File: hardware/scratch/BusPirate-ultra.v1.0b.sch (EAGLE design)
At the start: 164 parts, among them IC1 IC_MEM_23LC1024, IC10 IC_BUFF_SN74LVC1T45DBV, IC11 IC_BUFF_SN74LVC1T45DBV, IC12 74LVC1G07DBV, IC13 IC_BUFF_SN74LVC1T45DBV, IC17 74LVC1G07DBV, IC18 IC_BUFF_SN74LVC1T45DBV, IC19 74LVC1G07DBV, IC2 IC_MEM_23LC1024, IC20 IC_BUFF_SN74LVC1T45DBV, IC21 74LVC1G07DBV, IC22 IC_BUFF_SN74LVC1T45DBV, IC23 MCP1824_ADJ, IC24 74HCT4051, IC3 IC_74AC573, IC4 74LVC1G07DBV, IC5 74LVC1G07DBV, IC6 74LVC1G07DBV, IC7 74LVC1G07DBV, IC8 SN74LVC1T45DBV, IC9 IC_BUFF_SN74LVC1T45DBV, J1 CON_HEADER_2X02-PTH, J2 CON_HEADER_1X04, J3 CON_HEADER_1X03-PTH, J4 CON_HEADER_1X10-RIGHT_ANGLED_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, Q1 DMMT3906W, U1 W25X40CL, U2 IC_UC_STM32F103ZX, U3 IC_FPGA_ICE40HX4K, U4 MCP6001, U5 MCP4442, U6 MCP4442

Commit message: fix placement
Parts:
- IC10, IC11, IC13, IC18, IC20, IC22, IC9: value IC_BUFF_SN74LVC1T45DBV -> SN74LVC1T45DBV
- U2: value IC_UC_STM32F103ZX -> STM32F103ZX
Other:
- note added: "FLASH STORAGE"
- note removed: "LA_LAT_MISO -> BPIO_MISO"
- moved on the sheet: C1, C10, C11, C12, C13, C14, C15, C16, C17, C18, C19, C2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

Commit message: changes are.. -fix schematic placements -wired latch chip to BP IO and fix net names -SRAM chip CS pin connected to ARM chip -flipped connection of BP IO, MOSI now on pin 1, GND on pin 10... etc -removed reset button -removed boot mode jumper config pins -buffer Vb connected to Vref/Vout -UART pins changed to test pads -EEPROM pins breakout to pads -ADC/Analog mux control pins wired to FPGA
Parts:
- removed J1: CON_HEADER_2X02-PTH, dp_devices:CON_HEADER_2X02-PTH
- removed J3: CON_HEADER_1X03-PTH, dp_devices.v6:CON_HEADER_1X03-PTH
- removed SW1: (no value), dp_devices.v6:SW_TACT_4P
- added C51: 1uF, rcl:C-EUC0603
- added D1: (no value), dp_devices.v6:DIODE-SOD-123
- added R50, R51: (no value), resistor:R-EU_R0603
- added TP1, TP2, TP3, TP4, TP5, TP6, TP7, TP8: TPB1,27, testpad:TPB1,27
- added U7: MCP6001, dp_devices.v6:IC_MCP6001
- IC1, IC2: value IC_MEM_23LC1024 -> 23LC1024
- IC3: value IC_74AC573 -> 74AC573
- U3: value IC_FPGA_ICE40HX4K -> ICE40HX4K
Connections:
- net LAT_SWV33 renamed LAT_AUX2
- net LAT_SWV50 renamed LAT_AUX3
- removed net BPIO_AUX: IC3IC.6D
- removed net LAT_CLK: IC3IC.3Q, U3BANK1.GBIN2/IOR_141
- removed net SWV33: IC3IC.7D
- removed net SWV50: IC3IC.8D
- removed net VPUN: C45.2, C46.2, C47.2, C48.2, C49.2, C56.2, C58.2, C60.2, IC10.VCCB, IC11.VCCB, IC13.VCCB, IC18.VCCB, IC20.VCCB, IC22.VCCB, IC8.VCCB, IC9.VCCB
- new net ADC_MUX_EN: IC24.!E, U3BANK2.IOB_73
- new net FLASH_CS: TP7.TP, U1.!CS, U2U.PG15/FT
- new net LAT_CLOCK: IC3IC.2Q, U3BANK1.GBIN3/IOR_140
- new net N$64: R51.1, U7.-, U7.OUT
- new net N$65: R51.2, R9.1
- net 3V3: no longer J1.2, J1.4, U1.!CS
- net ADC_MUX_S0: now also U3BANK2.IOB_64
- net ADC_MUX_S1: now also U3BANK2.IOB_71
- net ADC_MUX_S2: now also U3BANK2.IOB_72
- net BOOT0: no longer J1.1
- net BOOT1: no longer J1.3
- net BPIO_AUX0: now also IC3IC.5D, J4.5; no longer J4.6
- net BPIO_AUX1: now also IC3IC.6D, J4.6; no longer J4.5
- net BPIO_AUX2: now also IC3IC.7D, J4.7; no longer J4.4
- net BPIO_AUX3: now also IC3IC.8D, J4.8; no longer J4.3
- net BPIO_CLOCK: now also IC3IC.2D, J4.2; no longer IC3IC.3D, J4.9
- net BPIO_CS: now also IC3IC.4D, J4.4; no longer IC3IC.5D, J4.7
- net BPIO_MISO: now also IC3IC.3D, J4.3; no longer IC3IC.4D, J4.8
- net BPIO_MOSI: now also IC3IC.1D, J4.1; no longer IC3IC.2D, J4.10
- net FLASH_MISO: now also TP5.TP
- net FLASH_MOSI: now also TP4.TP
- net FLASH_SCK: now also TP6.TP
- net GND: now also C14.2, C51.2, IC24.VEE, J4.10, TP1.TP, TP8.TP, U7.V-; no longer C14.1, IC3IC.1D, J3.1, J4.1, SW1.3, SW1.4
- net LAT_AUX0: now also IC3IC.5Q, U3BANK1.IOR_146; no longer IC3IC.6Q, U3BANK1.IOR_147
- net LAT_AUX1: now also IC3IC.6Q, U3BANK1.IOR_147; no longer IC3IC.1Q, U3BANK1.IOR_139
- net LAT_CS: now also IC3IC.4Q, U3BANK1.IOR_144; no longer IC3IC.5Q, U3BANK1.IOR_146
- net LAT_MISO: now also IC3IC.3Q, U3BANK1.GBIN2/IOR_141; no longer IC3IC.4Q, U3BANK1.IOR_144
- net LAT_MOSI: now also IC3IC.1Q, U3BANK1.IOR_139; no longer IC3IC.2Q, U3BANK1.GBIN3/IOR_140
- net N$32: now also D1.A, R50.2, U7.+; no longer IC24.Z, R9.1
- net N$61: now also IC24.Z, R50.1; no longer U2U.PG15/FT
- net RST: no longer C14.2, SW1.1, SW1.2
- net UART_RX: now also TP2.TP; no longer J3.2
- net UART_TX: now also TP3.TP; no longer J3.3
- net VREF/VOUT: now also C45.2, C46.2, C47.2, C48.2, C49.2, C56.2, C58.2, C60.2, IC10.VCCB, IC11.VCCB, IC13.VCCB, IC18.VCCB, IC20.VCCB, IC22.VCCB, IC8.VCCB, IC9.VCCB, J4.9; no longer J4.2
- net VUSB: now also C14.1, C51.1, D1.C, U7.V+
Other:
- note added: "ADC MUX + Analog buffer"
- note added: "EEPROM"
- note added: "EEPROM TEST PADS"
- note removed: "ADC SENSE"
- note removed: "BOOT MODE"
- note removed: "FLASH STORAGE"
- note removed: "RESET"
- moved on the sheet: C1, C10, C11, C12, C13, C14, C15, C16, C17, C18, C19, C2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

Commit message: change BP IO to a more universal naming
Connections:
- net BPIO_AUX0 renamed BPIO4
- net BPIO_AUX1 renamed BPIO5
- net BPIO_AUX2 renamed BPIO6
- net BPIO_AUX3 renamed BPIO7
- net BPIO_CLOCK renamed BPIO1
- net BPIO_CS renamed BPIO3
- net BPIO_MISO renamed BPIO2
- net BPIO_MOSI renamed BPIO0
- net BUFDIR_AUX0 renamed BUFDIR4
- net BUFDIR_CLOCK renamed BUFDIR1
- net BUFDIR_CS renamed BUFDIR3
- net BUFDIR_MISO renamed BUFDIR2
- net BUFDIR_MOSI renamed BUFDIR0
- net BUFIO_AUX0 renamed BUFIO4
- net BUFIO_CLOCK renamed BUFIO1
- net BUFIO_CS renamed BUFIO3
- net BUFIO_MISO renamed BUFIO2
- net BUFIO_MOSI renamed BUFIO0
- net BUFOD_AUX0 renamed BUFOD4
- net BUFOD_CLOCK renamed BUFOD1
- net BUFOD_CS renamed BUFOD3
- net BUFOD_MISO renamed BUFOD2
- net BUFOD_MOSI renamed BUFOD0

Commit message: route new vreg circuit
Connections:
- net !SHDN renamed VREG_EN
- new net VREG_PWM: R48.2
- net PWM: no longer R48.2
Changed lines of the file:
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@@
 <label x="147.32" y="370.84" size="1.778" layer="95" align="center-left"/>
-</segment>
-<segment>
-<pinref part="R48" gate="R" pin="2"/>
-<label x="307.34" y="292.1" size="1.778" layer="95" align="center-right"/>
-<wire x1="309.88" y1="292.1" x2="307.34" y2="292.1" width="0.1524" layer="91"/>
 </segment>
 </net>
@@
 </segment>
 </net>
-<net name="!SHDN" class="0">
+<net name="VREG_EN" class="0">
 <segment>
 <pinref part="IC23" gate="IC" pin="!SHDN"/>
@@
 </segment>
 </net>
+<net name="VREG_PWM" class="0">
+<segment>
+<pinref part="R48" gate="R" pin="2"/>
+<label x="307.34" y="292.1" size="1.778" layer="95" align="center-right"/>
+<wire x1="309.88" y1="292.1" x2="307.34" y2="292.1" width="0.1524" layer="91"/>
+</segment>
+</net>

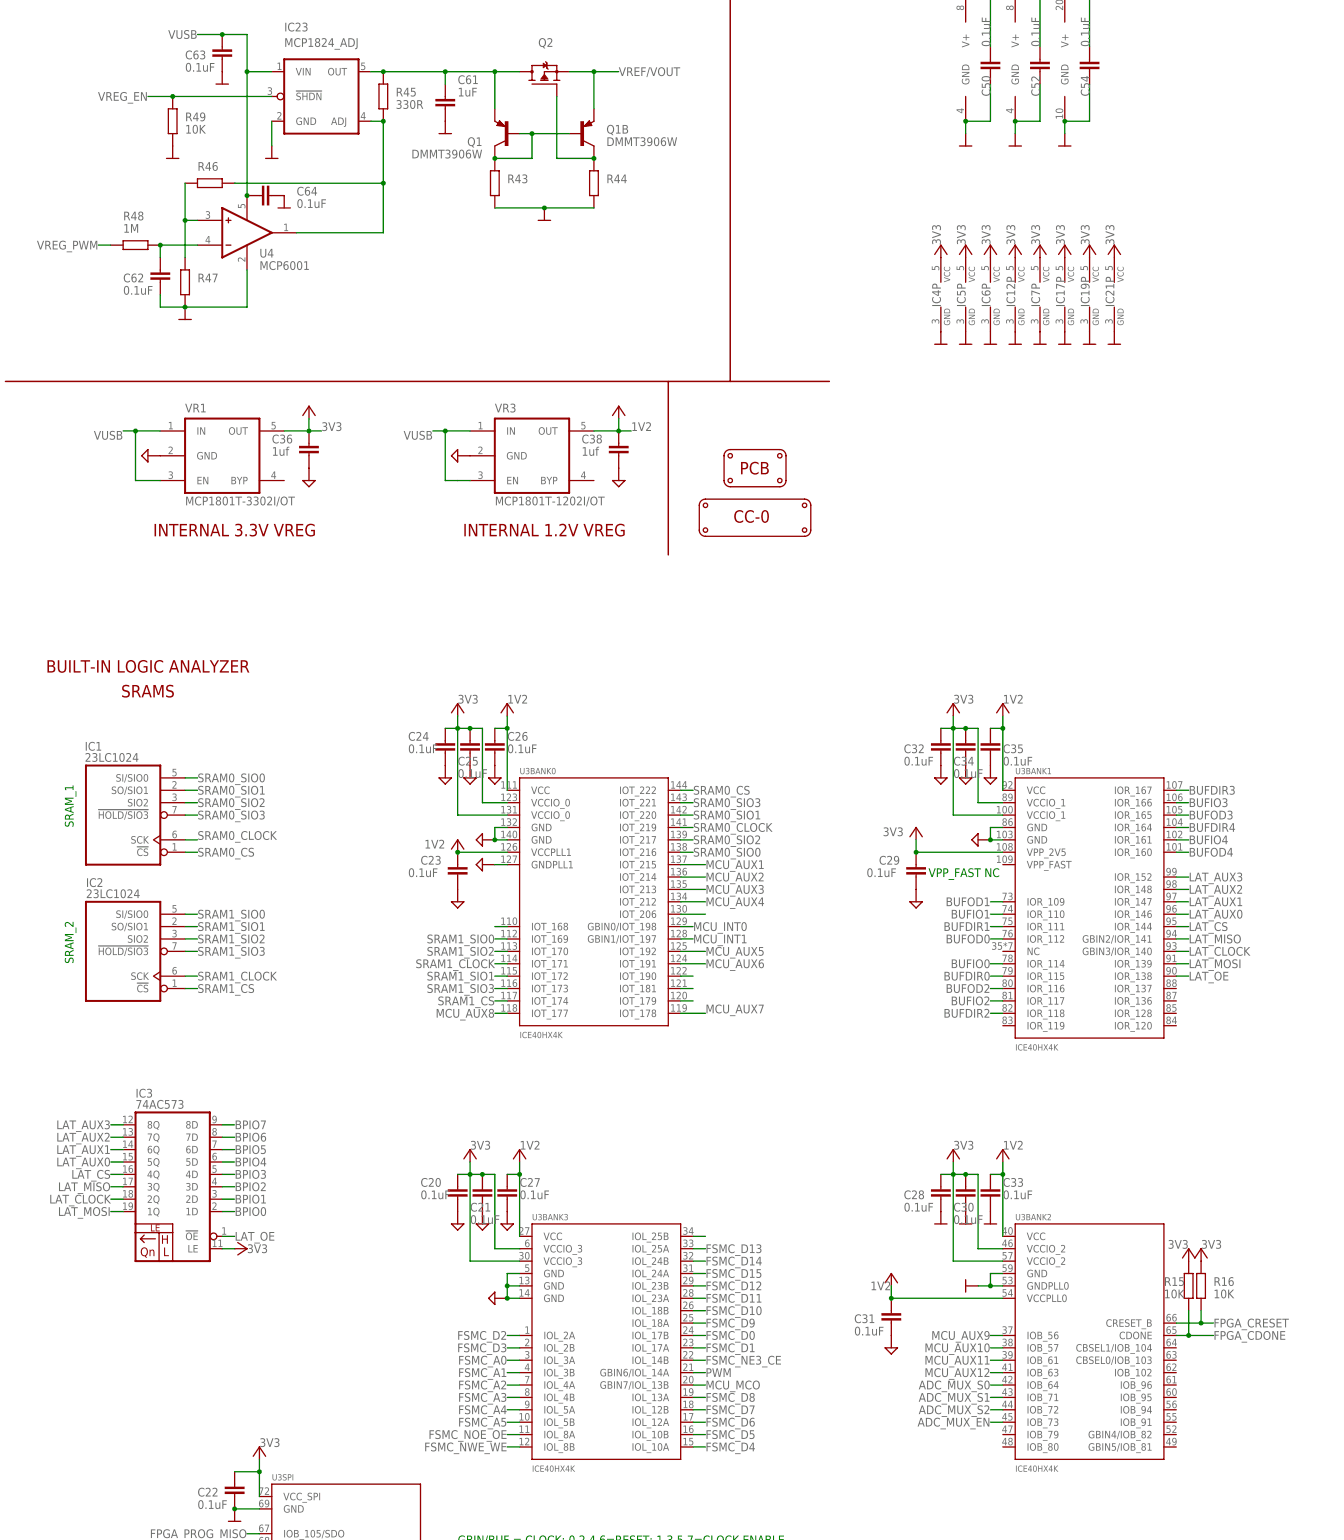
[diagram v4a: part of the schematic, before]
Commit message: move things around, move MCU_INT1 to GBIN5 and MCU_MCO to GBIN1, fix VREGEN and VREG_EN
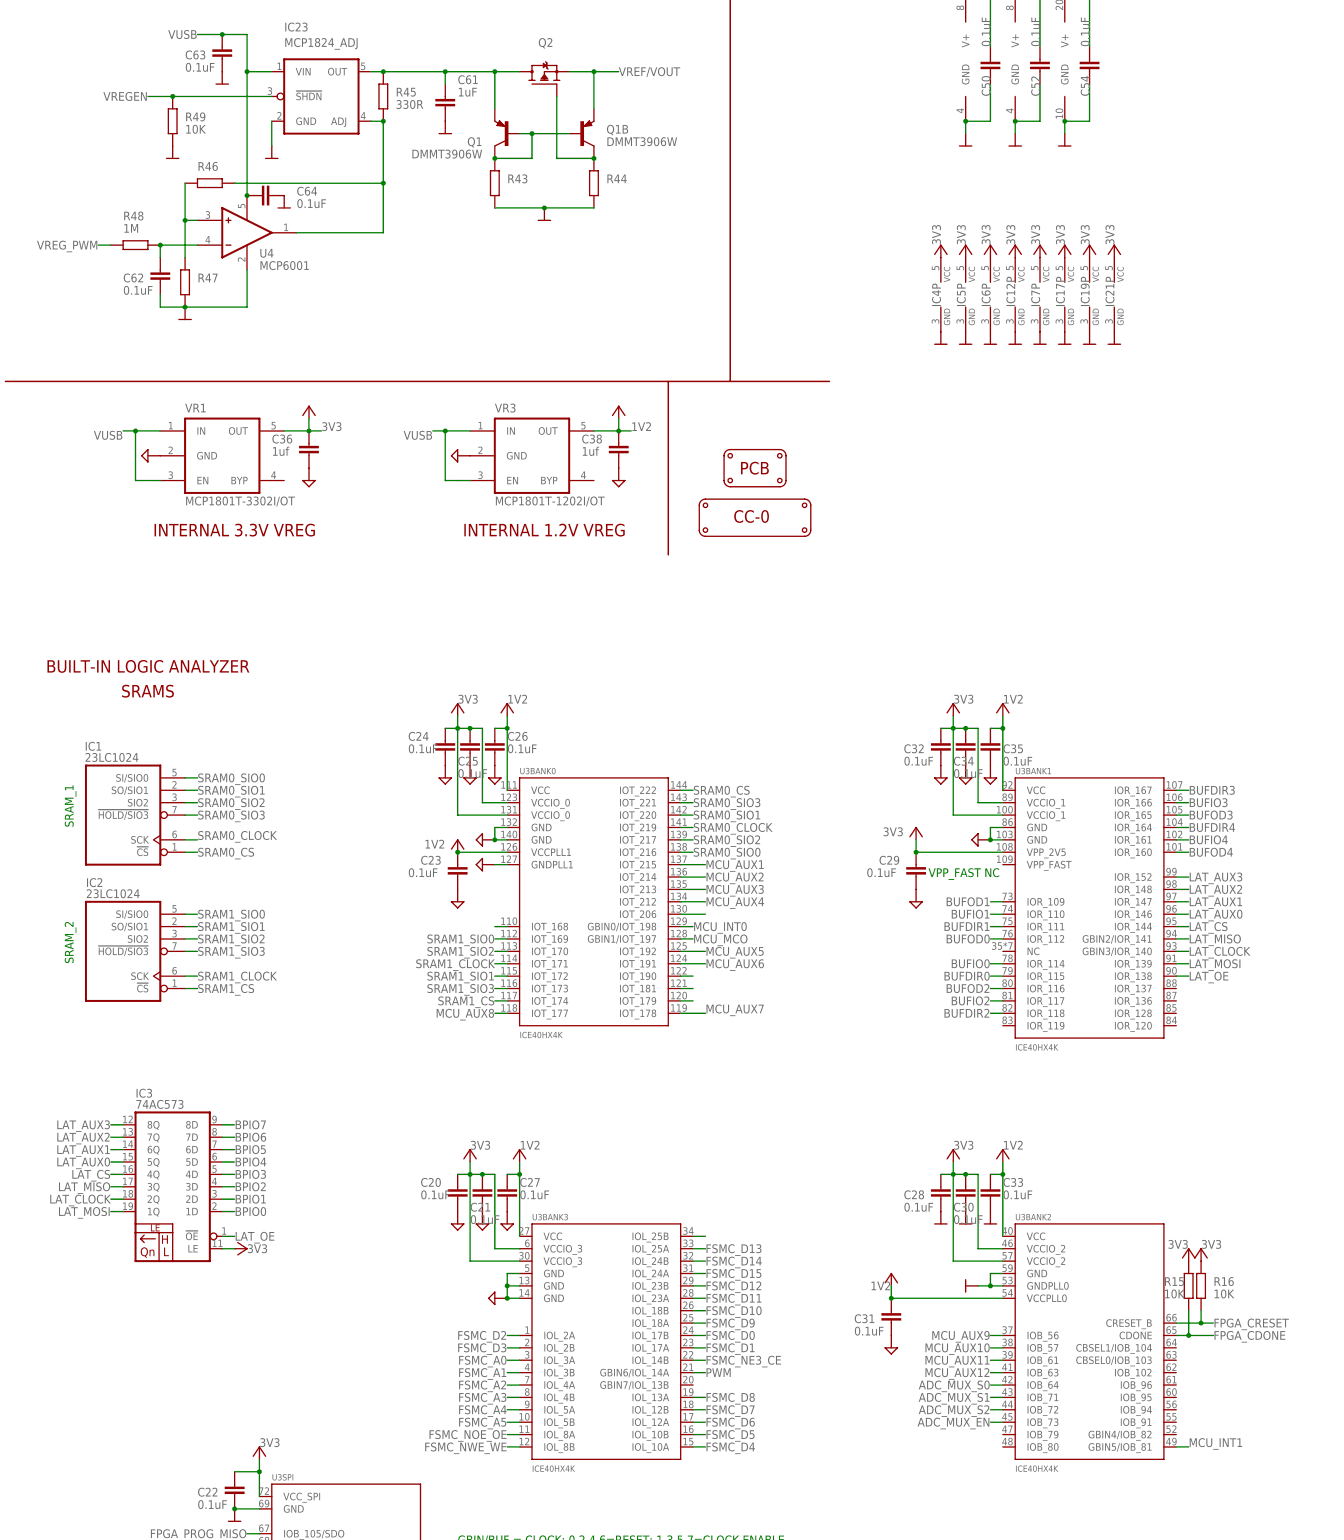
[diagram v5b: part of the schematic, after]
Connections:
- removed net VREG_EN: IC23.!SHDN, R49.1
- net MCU_INT1: now also U3BANK2.GBIN5/IOB_81; no longer U3BANK0.GBIN1/IOT_197
- net MCU_MCO: now also U3BANK0.GBIN1/IOT_197; no longer U3BANK3.GBIN7/IOL_13B
- net VREGEN: now also IC23.!SHDN, R49.1
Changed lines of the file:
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@@
 <?xml version="1.0" encoding="utf-8"?>
 <!DOCTYPE eagle SYSTEM "eagle.dtd">
-<eagle version="9.4.2">
+<eagle version="9.1.3">
 <drawing>
 <settings>
@@
 <junction x="162.56" y="307.34"/>
 </segment>
+<segment>
+<pinref part="IC23" gate="IC" pin="!SHDN"/>
+<wire x1="342.9" y1="322.58" x2="322.58" y2="322.58" width="0.1524" layer="91"/>
+<wire x1="322.58" y1="322.58" x2="317.5" y2="322.58" width="0.1524" layer="91"/>
+<pinref part="R49" gate="R" pin="1"/>
+<junction x="322.58" y="322.58"/>
+<label x="317.5" y="322.58" size="1.778" layer="95" align="center-right"/>
+</segment>
 </net>
 <net name="N$18" class="0">
@@
 <net name="MCU_INT1" class="0">
 <segment>
-<pinref part="U3" gate="BANK0" pin="GBIN1/IOT_197"/>
-<wire x1="426.72" y1="149.86" x2="429.26" y2="149.86" width="0.1524" layer="91"/>
-<label x="429.26" y="149.86" size="1.778" layer="95" align="center-left"/>
-</segment>
-<segment>
 <pinref part="U2" gate="U" pin="PE3/FT/FSMC_A19"/>
 <wire x1="38.1" y1="335.28" x2="35.56" y2="335.28" width="0.1524" layer="91"/>
 <label x="35.56" y="335.28" size="1.778" layer="95" align="center-right"/>
 </segment>
+<segment>
+<pinref part="U3" gate="BANK2" pin="GBIN5/IOB_81"/>
+<wire x1="528.32" y1="45.72" x2="530.86" y2="45.72" width="0.1524" layer="91"/>
+<label x="530.86" y="45.72" size="1.778" layer="95"/>
+</segment>
 </net>
 <net name="PWM" class="0">
@@
 </segment>
 <segment>
-<pinref part="U3" gate="BANK3" pin="GBIN7/IOL_13B"/>
-<wire x1="429.26" y1="58.42" x2="431.8" y2="58.42" width="0.1524" layer="91"/>
-<label x="431.8" y="58.42" size="1.778" layer="95" align="center-left"/>
+<pinref part="U3" gate="BANK0" pin="GBIN1/IOT_197"/>
+<wire x1="426.72" y1="149.86" x2="429.26" y2="149.86" width="0.1524" layer="91"/>
+<label x="429.26" y="149.86" size="1.778" layer="95" align="center-left"/>
 </segment>
 </net>
@@
 </segment>
 </net>
-<net name="VREG_EN" class="0">
-<segment>
-<pinref part="IC23" gate="IC" pin="!SHDN"/>
-<wire x1="342.9" y1="322.58" x2="322.58" y2="322.58" width="0.1524" layer="91"/>
-<wire x1="322.58" y1="322.58" x2="317.5" y2="322.58" width="0.1524" layer="91"/>
-<pinref part="R49" gate="R" pin="1"/>
-<junction x="322.58" y="322.58"/>
-<label x="317.5" y="322.58" size="1.778" layer="95" align="center-right"/>
-</segment>
-</net>

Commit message: below are the changes in the schematic -remove extra pull-down resistor on VREGEN -BOOT0 and BOOT1 now connect directly to GND -change latch nets naming scheme -add divider resistors to sense voltage to Vout/Vref -renamed the control pins of the rest of the buffers -move UART to USART1 (PA9 and PA10) -connect digital pot to ARM's I2C1 (PB6 and PB7) with their pull-ups resistors, A0 and A1 wired to (PE5 and PE6) -all ADC Mux control lines are controlled only by FPGA -flip the order of latch connection of FPGA
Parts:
- added R52: 10K, dp_devices.v6:RESISTOR-0603
- R4: device dp_devices:RESISTOR-0603 -> dp_devices.v6:RESISTOR-0603
- R7, R8: device rcl:R-EU_R0603 -> resistor:R-EU_R0603
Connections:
- net ADC5 renamed MCU_ADC5
- net LAT_AUX0 renamed LAT3
- net LAT_AUX1 renamed LAT2
- net LAT_AUX2 renamed LAT1
- net LAT_AUX3 renamed LAT0
- net LAT_CLOCK renamed LAT6
- net LAT_CS renamed LAT4
- net LAT_MISO renamed LAT5
- net LAT_MOSI renamed LAT7
- removed net BOOT0: R8.1, U2U.BOOT0
- removed net BOOT1: R7.1, U2U.BOOT1/FT/PB2
- removed net BUFDIR_AUX1: IC18.DIR, R35.2
- removed net BUFDIR_AUX2: IC20.DIR, R38.2
- removed net BUFDIR_AUX3: IC22.DIR, R41.2
- removed net BUFIO_AUX1: IC18.A
- removed net BUFIO_AUX2: IC20.A
- removed net BUFIO_AUX3: IC22.A
- removed net BUFOD_AUX1: IC17A.I, R34.1
- removed net BUFOD_AUX2: IC19A.I, R37.1
- removed net BUFOD_AUX3: IC21A.I, R40.1
- removed net N$31: U5.A1
- removed net N$33: U5.HVC/A0
- removed net N$45: U2U.PA10/FT/USART1_RX('0')/TIM1_CH3('00'OR'01')
- removed net N$46: U2U.PA9/FT/USART1_TX('0')/TIM1_CH2('00'OR'01')
- removed net N$49: U5.SCL
- removed net N$50: U5.SDA
- removed net N$51: U6.A1
- removed net N$55: U6.HVC/A0
- removed net N$62: U6.SCL
- removed net N$63: U6.SDA
- new net BUFDIR5: IC18.DIR, R35.2, U3BANK1.IOR_137
- new net BUFDIR6: IC20.DIR, R38.2, U3BANK2.IOB_96
- new net BUFDIR7: IC22.DIR, R41.2, U3BANK2.CBSEL1/IOB_104
- new net BUFIO5: IC18.A, U3BANK1.IOR_136
- new net BUFIO6: IC20.A, U3BANK2.IOB_95
- new net BUFIO7: IC22.A, U3BANK2.CBSEL0/IOB_103
- new net BUFOD5: IC17A.I, R34.1, U3BANK1.IOR_128
- new net BUFOD6: IC19A.I, R37.1, U3BANK2.IOB_94
- new net BUFOD7: IC21A.I, R40.1, U3BANK2.IOB_102
- new net MCU_ADC6: R7.2, R8.2, U2U.PA2/USART2_TX('0')/TIM5_CH3/ADC123_IN2/TIM2_CH3('00'OR'01)
- new net MCU_I2C_A0: U2U.PE5/FT/FSMC_A21, U5.HVC/A0, U6.HVC/A0
- new net MCU_I2C_A1: U2U.PE6/FT/FSMC_A22, U5.A1, U6.A1
- new net MCU_I2C_SCL: R49.1, U2U.I2C1_SCL('0')/TIM4_CH1('0')/USART1_TX('1')/FT/PB6, U5.SCL, U6.SCL
- new net MCU_I2C_SDA: R52.1, U2U.I2C1_SDA('0')/FSMC_NADV/TIM4_CH2('0')/USART1_RX('1')/FT/PB7, U5.SDA, U6.SDA
- net 3V3: now also R49.2, R52.2
- net ADC_MUX_S0: no longer U2U.PG2/FT/FSMC_A12
- net ADC_MUX_S1: no longer U2U.PG3/FT/FSMC_A13
- net ADC_MUX_S2: no longer U2U.PG4/FT/FSMC_A14
- net BPIO0: now also IC3IC.8D; no longer IC3IC.1D
- net BPIO1: now also IC3IC.7D; no longer IC3IC.2D
- net BPIO2: now also IC3IC.6D; no longer IC3IC.3D
- net BPIO3: now also IC3IC.5D; no longer IC3IC.4D
- net BPIO4: now also IC3IC.4D; no longer IC3IC.5D
- net BPIO5: now also IC3IC.3D; no longer IC3IC.6D
- net BPIO6: now also IC3IC.2D; no longer IC3IC.7D
- net BPIO7: now also IC3IC.1D; no longer IC3IC.8D
- net GND: now also R8.1, U2U.BOOT0, U2U.BOOT1/FT/PB2; no longer R49.2, R7.2, R8.2
- net N$29: now also U2U.PD2/FT/TIM3_ETR/UART5_RX; no longer U2U.PA2/USART2_TX('0')/TIM5_CH3/ADC123_IN2/TIM2_CH3('00'OR'01)
- net UART_RX: now also U2U.PA10/FT/USART1_RX('0')/TIM1_CH3('00'OR'01'); no longer U2U.I2C1_SDA('0')/FSMC_NADV/TIM4_CH2('0')/USART1_RX('1')/FT/PB7
- net UART_TX: now also U2U.PA9/FT/USART1_TX('0')/TIM1_CH2('00'OR'01'); no longer U2U.I2C1_SCL('0')/TIM4_CH1('0')/USART1_TX('1')/FT/PB6
- net VREF/VOUT: now also R7.1
- net VREGEN: no longer R49.1
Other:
- note removed: "need to connect I2C"
- note removed: "tentative placement"
- moved on the sheet: C61, C62, C63, C64, IC23, Q1, Q1B, Q2, R43, R44, R45, R46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

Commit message: fix digital pots address lines voltage reg DAC buffer opamp (MCP6001), shorted the feedback, change R45 value to 100K, remove C62, added devider resistors R47(78.7K) and R46(50K), removed input resistor R48, add input cap initial change to small package (SC-70, 0402) IO-0 buffer
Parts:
- removed C62: 0.1uF, dp_devices.v6:CAPACITOR_NPOL-0603
- removed R48: 1M, dp_devices.v6:RESISTOR-0603
- added C53: (no value), dp_devices.v6:CAPACITOR_NPOL-0603
- C39, C45: device rcl:C-EUC0603 -> rcl:C-EUC0402
- IC4: device 74xx-little-de:74LVC1G07DBV -> dp_devices.v6:IC_BUFF_74LVC1G07
- IC8: device dp_devices.v6:IC_BUFF_SN74LVC1T45DBV -> dp_devices.v6:IC_BUFF_SN74LVC1T45DBV-SC-70-6
- R19, R24, R28: device rcl:R-EU_R0603 -> rcl:R-EU_R0402
- R45: value 330R -> 100K
- R46: value (none) -> 50K
- R47: value (none) -> 78.7K
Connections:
- removed net ADC3: U2U.PA5/SPI1_SCK('0')/ADC12_IN5
- removed net ADC4: U2U.PA4/SPI1_NSS('0')/USART2_CK('0')/ADC12_IN4
- removed net MCU_I2C_A0: U2U.PE5/FT/FSMC_A21, U5.HVC/A0, U6.HVC/A0
- removed net MCU_I2C_A1: U2U.PE6/FT/FSMC_A22, U5.A1, U6.A1
- removed net N$15: R46.2, R47.1, U4.+
- removed net VREG_PWM: R48.2
- new net VREG_DAC: C53.1, U2U.PA4/SPI1_NSS('0')/USART2_CK('0')/ADC12_IN4, U4.+
- net 3V3: now also IC4P.V+, U6.HVC/A0; no longer IC4P.VCC
- net BPIO0: now also IC4G.O; no longer IC4A.O
- net BUFOD0: now also IC4G.I; no longer IC4A.I
- net GND: now also C53.2, R46.2, U5.A1, U5.HVC/A0, U6.A1; no longer C62.2, R47.2
- net N$12: now also R47.2; no longer U4.OUT
- net N$25: now also R47.1, U4.OUT; no longer C62.1, R48.1
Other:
- moved on the sheet: C64, IC4P, R46, R47, U4
